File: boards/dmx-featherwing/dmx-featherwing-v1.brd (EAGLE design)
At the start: 50.8 x 22.9 mm, 8 parts, among them J1 5520251-4, U1 SN65HVD11D

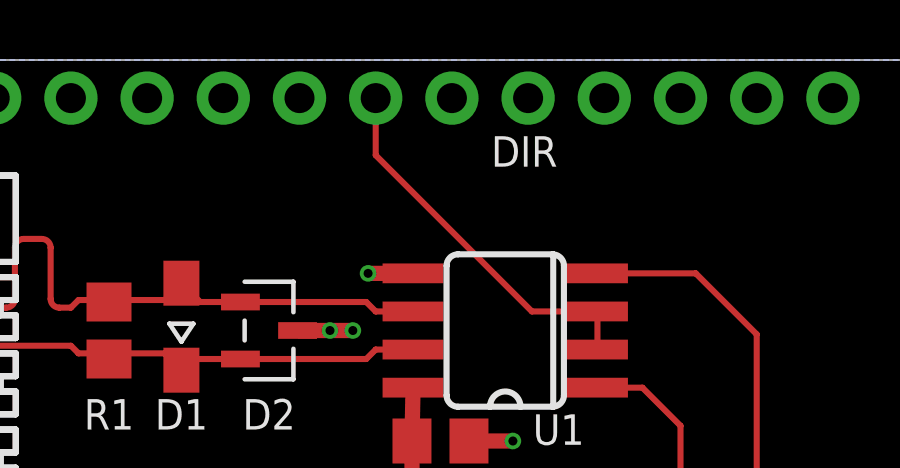
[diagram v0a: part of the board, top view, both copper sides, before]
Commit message: fixed R1 name/value, moved DIR label to correct pin
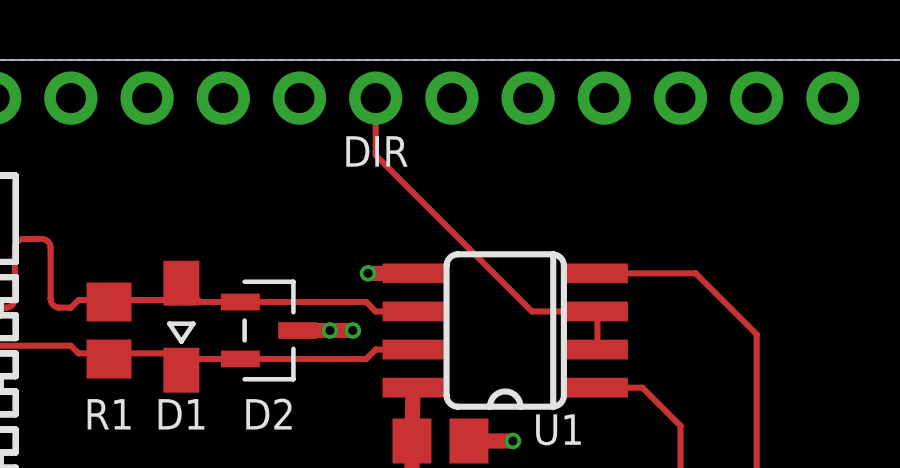
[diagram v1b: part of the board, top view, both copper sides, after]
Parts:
- R1: value (none) -> 120
- renumbered 120 to R1
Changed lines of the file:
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@@
 <text x="39.37" y="2.54" size="1.016" layer="121" font="vector" ratio="16" align="bottom-center">RX</text>
 <text x="41.91" y="2.54" size="1.016" layer="121" font="vector" ratio="16" align="bottom-center">TX</text>
-<text x="34.163" y="20.32" size="1.016" layer="121" font="vector" ratio="16" rot="R180" align="bottom-center">DIR</text>
+<text x="29.21" y="20.32" size="1.016" layer="121" font="vector" ratio="16" rot="R180" align="bottom-center">DIR</text>
 <text x="4.699" y="19.304" size="1.016" layer="121" font="vector" ratio="16">J1</text>
 <text x="22.733" y="11.557" size="1.016" layer="121" font="vector" ratio="16" rot="R180" align="bottom-center">D1</text>
@@
 </element>
 <element name="C2" library="rcl" package="C1206K" value="1000pF 2kV" x="10.287" y="21.082" smashed="yes" rot="R180"/>
-<element name="120" library="rcl" package="R0805" value="" x="20.32" y="13.843" smashed="yes" rot="R270">
+<element name="R1" library="rcl" package="R0805" value="120" x="20.32" y="13.843" smashed="yes" rot="R270">
 <attribute name="VALUE" x="17.78" y="14.478" size="1.27" layer="27" rot="R270"/>
 </element>
@@
 <wire x1="28.895" y1="12.893" x2="29.21" y2="13.208" width="0.2032" layer="1"/>
 <wire x1="29.21" y1="13.208" x2="30.4546" y2="13.208" width="0.2032" layer="1"/>
-<contactref element="120" pad="2"/>
+<contactref element="R1" pad="2"/>
 <wire x1="20.32" y1="12.893" x2="20.32" y2="13.081" width="0.508" layer="1"/>
 </signal>
@@
 <wire x1="28.895" y1="14.793" x2="29.21" y2="14.478" width="0.2032" layer="1"/>
 <wire x1="29.21" y1="14.478" x2="30.4546" y2="14.478" width="0.2032" layer="1"/>
-<contactref element="120" pad="1"/>
+<contactref element="R1" pad="1"/>
 <wire x1="20.32" y1="14.793" x2="20.32" y2="14.859" width="0.508" layer="1"/>
 </signal>
